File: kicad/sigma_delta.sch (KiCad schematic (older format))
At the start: 26 parts, among them U1801 SI8661BD, U1802 SI8661BD

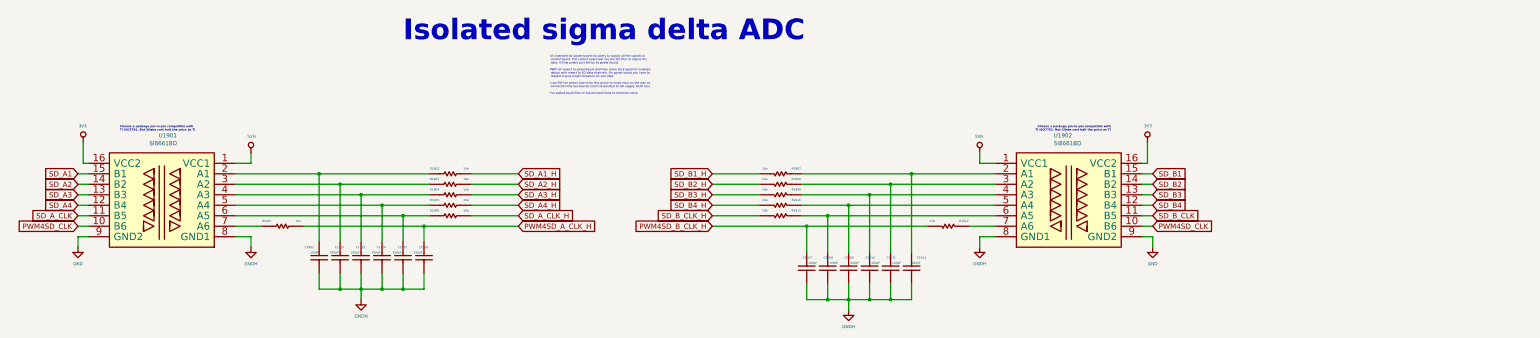
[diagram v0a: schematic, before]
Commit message: changing single row terminal block to double row
I've changed to double row all the connectors, RJ45 and terminal blocks,
I saves spaces and also make it more intuitive related to user
interface..lets go
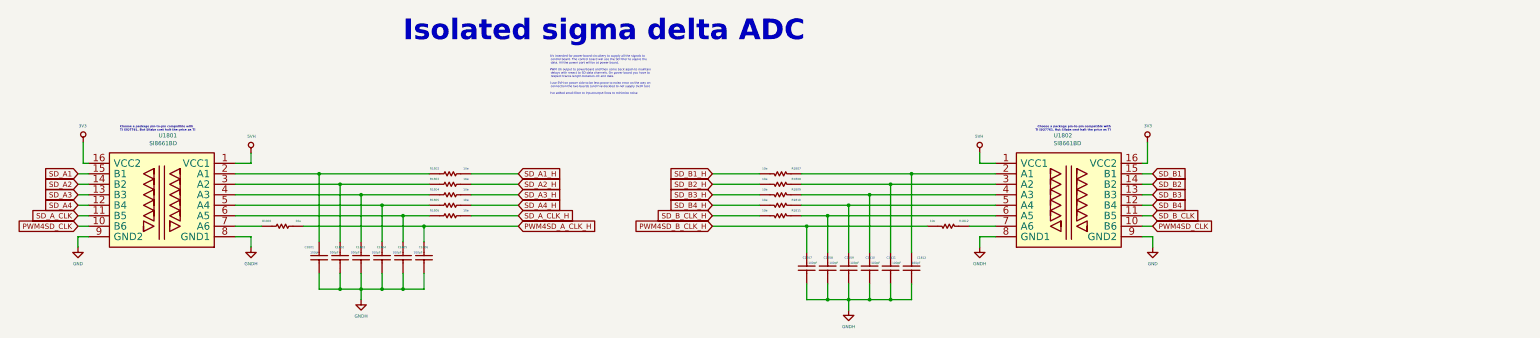
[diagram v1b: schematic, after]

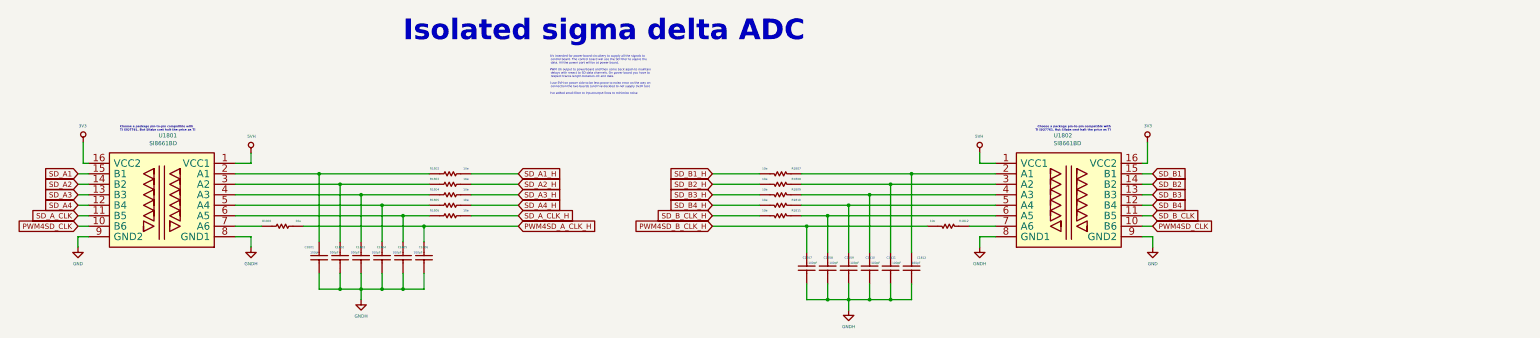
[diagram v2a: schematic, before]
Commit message: I forgot that QUEP was diferential!! all to back....
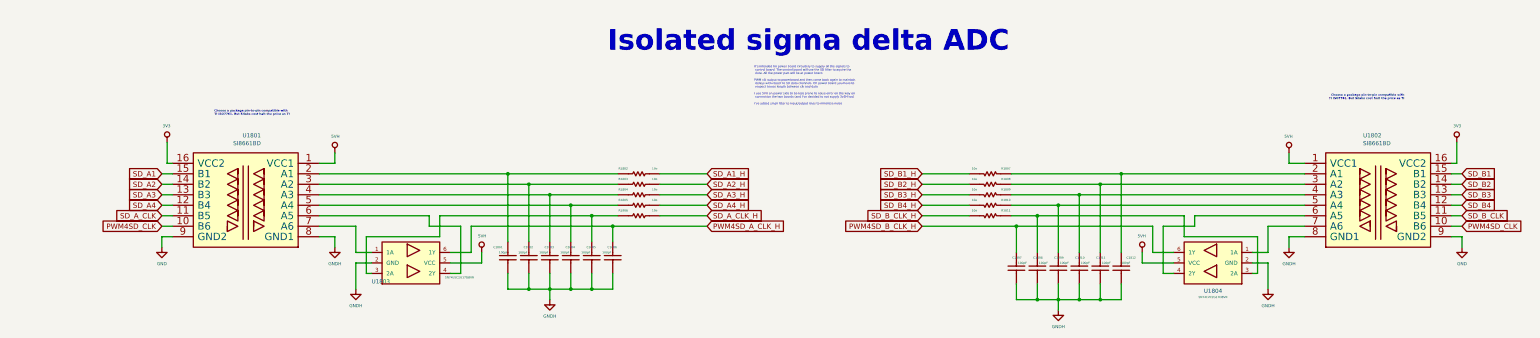
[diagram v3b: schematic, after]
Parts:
- removed R1801, R1812: 10e, Resistor_SMD:R_0603_1608Metric, symbol servo:Resistor
- added U1803, U1804: SN74LVC2G17DBVR, servo:SOT-23-6, symbol servo:SN74LVC2G17DBVR
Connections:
- net 5VH: now also U1803.5 (VCC), U1804.5 (VCC)
- net GNDH: now also U1803.2 (GND), U1804.2 (GND)
- net PWM4SD_A_CLK_H: now also U1803.6 (1Y)
- net PWM4SD_B_CLK_H: now also U1804.6 (1Y)
- net at C1805.1, R1806.1: now also U1803.3 (2A); no longer U1801.6 (A5)
- net at U1801.7 (A6): now also U1803.1 (1A)
- net at C1808.1, R1811.1: now also U1804.3 (2A); no longer U1802.6 (A5)
- net at U1802.7 (A6): now also U1804.1 (1A)
- new net: U1801.6 (A5), U1803.4 (2Y)
- new net: U1802.6 (A5), U1804.4 (2Y)
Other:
- moved on the sheet: C1801, C1802, C1803, C1804, C1805, C1806, C1807, C1808, C1809, C1810, C1811, C1812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

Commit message: placing smmall capacitors and resistors nerar his group
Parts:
- added C1813, C1814, C1815, C1816, C1817, C1818: 100pF, servo:C_0603_1608Metric, symbol servo:Capacitor
- added R1801, R1812: 10e, Resistor_SMD:R_0603_1608Metric, symbol servo:Resistor
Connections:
- net 3V3: now also C1813.1, C1818.1
- net 5VH: now also C1814.1, C1815.1, C1816.1, C1817.1
- net GND: now also C1813.2 (Capacitor), C1818.2 (Capacitor)
- net GNDH: now also C1814.2 (Capacitor), C1815.2 (Capacitor), C1816.2 (Capacitor), C1817.2 (Capacitor)
- net PWM4SD_A_CLK_H: now also R1801.2; no longer U1803.6 (1Y)
- net PWM4SD_B_CLK_H: now also R1812.2; no longer U1804.6 (1Y)
- new net: R1812.1, U1804.6 (1Y)
- new net: R1801.1, U1803.6 (1Y)
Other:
- moved on the sheet: C1806, C1807

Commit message: beginine routing... far far away
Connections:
- net PWM4SD_A_CLK_H renamed SD_CLK_OUT1_H
- net PWM4SD_B_CLK_H renamed SD_CLK_OUT2_H
- net PWM4SD_CLK renamed SD_CLK_OUT
- net SD_A1 renamed SD1_U
- net SD_A1_H renamed SD1_U_H
- net SD_A2 renamed SD1_V
- net SD_A2_H renamed SD1_V_H
- net SD_A3 renamed SD1_W
- net SD_A3_H renamed SD1_W_H
- net SD_A4 renamed SD1_A
- net SD_A4_H renamed SD1_A_H
- net SD_A_CLK renamed SD_CLK_IN1
- net SD_A_CLK_H renamed SD_CLK_IN1_H
- net SD_B1 renamed SD2_U
- net SD_B1_H renamed SD2_U_H
- net SD_B2 renamed SD2_V
- net SD_B2_H renamed SD2_V_H
- net SD_B3 renamed SD2_W
- net SD_B3_H renamed SD2_W_H
- net SD_B4 renamed SD2_A
- net SD_B4_H renamed SD2_A_H
- net SD_B_CLK renamed SD_CLK_IN2
- net SD_B_CLK_H renamed SD_CLK_IN2_H
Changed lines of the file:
@@
 Isolated sigma delta ADC
 Text GLabel 2700 3350 0    50   Input ~ 0
-SD_A_CLK
+SD_CLK_IN1
 $Comp
 L servo:GND #PWR?
@@
 	-1   0    0    -1
 $EndComp
-Text GLabel 2700 3450 0    50   Input ~ 0
-PWM4SD_CLK
 $Comp
 L servo:3V3 #PWR?
@@
 	2750 2650 2750 2850
 Text GLabel 2700 2950 0    50   Input ~ 0
-SD_A1
+SD1_U
 Text GLabel 2700 3050 0    50   Input ~ 0
-SD_A2
+SD1_V
 Text GLabel 2700 3150 0    50   Input ~ 0
-SD_A3
+SD1_W
 Text GLabel 2700 3250 0    50   Input ~ 0
-SD_A4
+SD1_A
 $Comp
 L servo:GNDH #PWR?
@@
 Wire Wire Line
 	7450 3350 7900 3350
-Text GLabel 15100 3350 2    50   Input ~ 0
-SD_B_CLK
 $Comp
 L servo:GND #PWR?
@@
 	1    0    0    -1
 $EndComp
-Text GLabel 15100 3450 2    50   Input ~ 0
-PWM4SD_CLK
 $Comp
 L servo:3V3 #PWR?
@@
 Wire Wire Line
 	15050 2650 15050 2850
-Text GLabel 15100 2950 2    50   Input ~ 0
-SD_B1
-Text GLabel 15100 3050 2    50   Input ~ 0
-SD_B2
-Text GLabel 15100 3150 2    50   Input ~ 0
-SD_B3
-Text GLabel 15100 3250 2    50   Input ~ 0
-SD_B4
 $Comp
 L servo:GNDH #PWR?
@@
 Wire Wire Line
 	11250 4250 11250 4150
-Text GLabel 7900 2950 2    50   Input ~ 0
-SD_A1_H
-Text GLabel 7900 3050 2    50   Input ~ 0
-SD_A2_H
-Text GLabel 7900 3150 2    50   Input ~ 0
-SD_A3_H
-Text GLabel 7900 3250 2    50   Input ~ 0
-SD_A4_H
-Text GLabel 7900 3350 2    50   Input ~ 0
-SD_A_CLK_H
-Text GLabel 7900 3450 2    50   Input ~ 0
-PWM4SD_A_CLK_H
-Text GLabel 9950 2950 0    50   Input ~ 0
-SD_B1_H
-Text GLabel 9950 3050 0    50   Input ~ 0
-SD_B2_H
-Text GLabel 9950 3150 0    50   Input ~ 0
-SD_B3_H
-Text GLabel 9950 3250 0    50   Input ~ 0
-SD_B4_H
-Text GLabel 9950 3350 0    50   Input ~ 0
-SD_B_CLK_H
-Text GLabel 9950 3450 0    50   Input ~ 0
-PWM4SD_B_CLK_H
 $Comp
 L servo:SN74LVC2G17DBVR U?
@@
 AR Path="/5EC40F3C/5E3CAD23" Ref="C?"  Part="1"
 AR Path="/6056AA11/5E3CAD23" Ref="C1818"  Part="1"
-F 0 "C1818" V 15400 2700 20  0000 R CNN
-F 1 "100pF" V 15350 2750 20  0000 R CNN
+F 0 "C1818" V 15322 2540 20  0000 R CNN
+F 1 "100pF" V 15279 2540 20  0000 R CNN
 F 2 "servo:C_0603_1608Metric" H 15250 2550 60  0001 C CNN
 F 3 "" H 15250 2650 60  0000 C CNN
@@
 AR Path="/6056AA11/5E3CAD30" Ref="#PWR0245"  Part="1"
 F 0 "#PWR0245" H 15250 2500 30  0001 C CNN
-F 1 "GND" H 15250 2592 30  0000 C CNN
+F 1 "GND" H 15150 2700 30  0000 C CNN
 F 2 "" H 15250 2750 50  0001 C CNN
 F 3 "" H 15250 2750 50  0001 C CNN
@@
 	1    0    0    -1
 $EndComp
+Text GLabel 2700 3450 0    50   Input ~ 0
+SD_CLK_OUT
+Text GLabel 15100 3350 2    50   Input ~ 0
+SD_CLK_IN2
+Text GLabel 15100 2950 2    50   Input ~ 0
+SD2_U
+Text GLabel 15100 3050 2    50   Input ~ 0
+SD2_V
+Text GLabel 15100 3150 2    50   Input ~ 0
+SD2_W
+Text GLabel 15100 3250 2    50   Input ~ 0
+SD2_A
+Text GLabel 15100 3450 2    50   Input ~ 0
+SD_CLK_OUT
+Text GLabel 9950 3350 0    50   Input ~ 0
+SD_CLK_IN2_H
+Text GLabel 9950 2950 0    50   Input ~ 0
+SD2_U_H
+Text GLabel 9950 3050 0    50   Input ~ 0
+SD2_V_H
+Text GLabel 9950 3150 0    50   Input ~ 0
+SD2_W_H
+Text GLabel 9950 3250 0    50   Input ~ 0
+SD2_A_H
+Text GLabel 9950 3450 0    50   Input ~ 0
+SD_CLK_OUT2_H
+Text GLabel 7900 3350 2    50   Input ~ 0
+SD_CLK_IN1_H
+Text GLabel 7900 2950 2    50   Input ~ 0
+SD1_U_H
+Text GLabel 7900 3050 2    50   Input ~ 0
+SD1_V_H
+Text GLabel 7900 3150 2    50   Input ~ 0
+SD1_W_H
+Text GLabel 7900 3250 2    50   Input ~ 0
+SD1_A_H
+Text GLabel 7900 3450 2    50   Input ~ 0
+SD_CLK_OUT1_H
 $EndSCHEMATC

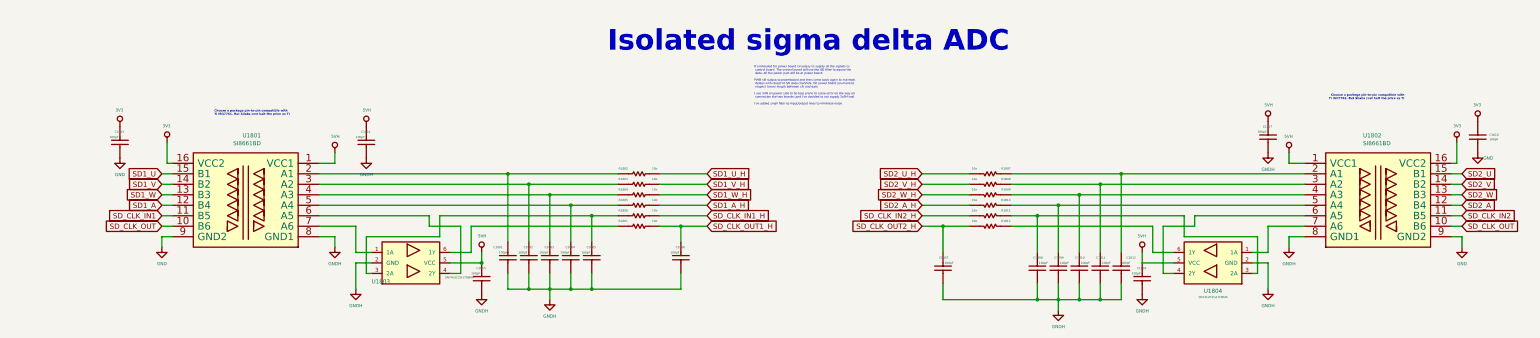
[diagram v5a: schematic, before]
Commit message: change in 5v interface scenario.. remove bridges
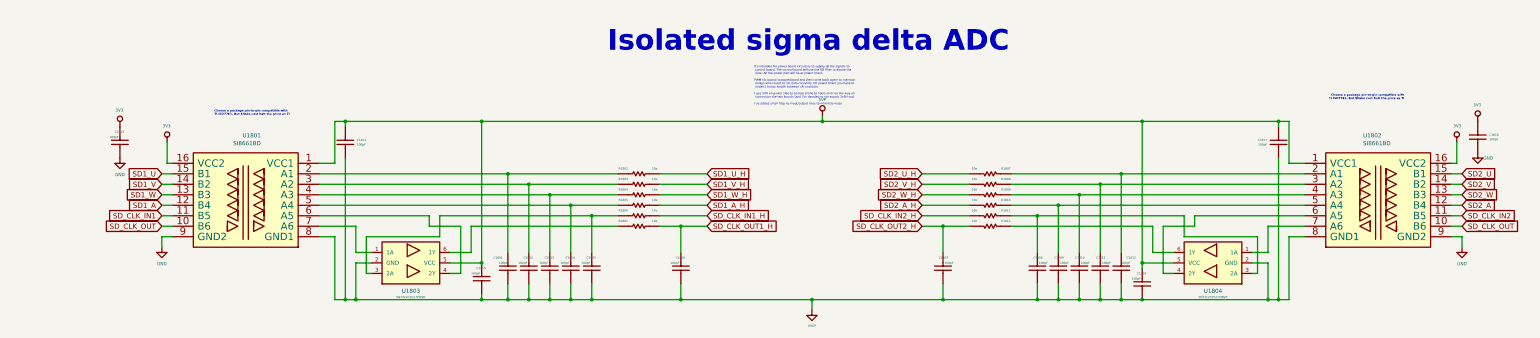
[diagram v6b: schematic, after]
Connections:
- net 5VH renamed 5VP
- net GNDH renamed GNDP
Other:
- moved on the sheet: C1801, C1802, C1803, C1804, C1805, C1806, C1814, C1816, C1817

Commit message: serigrafia...
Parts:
- R1801, R1802, R1803, R1804, R1805, R1806, R1807, R1808, R1809, R1810, R1811, R1812: footprint Resistor_SMD:R_0603_1608Metric -> servo:R_0603_1608Metric
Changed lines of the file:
@@
 F 0 "R1802" H 7100 3000 20  0000 C CNN
 F 1 "10e" H 7400 3000 20  0000 C CNN
-F 2 "Resistor_SMD:R_0603_1608Metric" H 6750 2850 60  0001 C CNN
+F 2 "servo:R_0603_1608Metric" H 6750 2850 60  0001 C CNN
 F 3 "" H 6850 2950 60  0001 C CNN
 	1    7250 2950
@@
 F 0 "R1803" H 7100 3100 20  0000 C CNN
 F 1 "10e" H 7400 3100 20  0000 C CNN
-F 2 "Resistor_SMD:R_0603_1608Metric" H 6750 2950 60  0001 C CNN
+F 2 "servo:R_0603_1608Metric" H 6750 2950 60  0001 C CNN
 F 3 "" H 6850 3050 60  0001 C CNN
 	1    7250 3050
@@
 F 0 "R1804" H 7100 3200 20  0000 C CNN
 F 1 "10e" H 7400 3200 20  0000 C CNN
-F 2 "Resistor_SMD:R_0603_1608Metric" H 6750 3050 60  0001 C CNN
+F 2 "servo:R_0603_1608Metric" H 6750 3050 60  0001 C CNN
 F 3 "" H 6850 3150 60  0001 C CNN
 	1    7250 3150
@@
 F 0 "R1805" H 7100 3300 20  0000 C CNN
 F 1 "10e" H 7400 3300 20  0000 C CNN
-F 2 "Resistor_SMD:R_0603_1608Metric" H 6750 3150 60  0001 C CNN
+F 2 "servo:R_0603_1608Metric" H 6750 3150 60  0001 C CNN
 F 3 "" H 6850 3250 60  0001 C CNN
 	1    7250 3250
@@
 F 0 "R1806" H 7100 3400 20  0000 C CNN
 F 1 "10e" H 7400 3400 20  0000 C CNN
-F 2 "Resistor_SMD:R_0603_1608Metric" H 6750 3250 60  0001 C CNN
+F 2 "servo:R_0603_1608Metric" H 6750 3250 60  0001 C CNN
 F 3 "" H 6850 3350 60  0001 C CNN
 	1    7250 3350
@@
 F 0 "R1807" H 10450 3000 20  0000 C CNN
 F 1 "10e" H 10750 3000 20  0000 C CNN
-F 2 "Resistor_SMD:R_0603_1608Metric" H 10100 2850 60  0001 C CNN
+F 2 "servo:R_0603_1608Metric" H 10100 2850 60  0001 C CNN
 F 3 "" H 10200 2950 60  0001 C CNN
 	1    10600 2950
@@
 F 0 "R1808" H 10450 3100 20  0000 C CNN
 F 1 "10e" H 10750 3100 20  0000 C CNN
-F 2 "Resistor_SMD:R_0603_1608Metric" H 10100 2950 60  0001 C CNN
+F 2 "servo:R_0603_1608Metric" H 10100 2950 60  0001 C CNN
 F 3 "" H 10200 3050 60  0001 C CNN
 	1    10600 3050
@@
 F 0 "R1809" H 10450 3200 20  0000 C CNN
 F 1 "10e" H 10750 3200 20  0000 C CNN
-F 2 "Resistor_SMD:R_0603_1608Metric" H 10100 3050 60  0001 C CNN
+F 2 "servo:R_0603_1608Metric" H 10100 3050 60  0001 C CNN
 F 3 "" H 10200 3150 60  0001 C CNN
 	1    10600 3150
@@
 F 0 "R1810" H 10450 3300 20  0000 C CNN
 F 1 "10e" H 10750 3300 20  0000 C CNN
-F 2 "Resistor_SMD:R_0603_1608Metric" H 10100 3150 60  0001 C CNN
+F 2 "servo:R_0603_1608Metric" H 10100 3150 60  0001 C CNN
 F 3 "" H 10200 3250 60  0001 C CNN
 	1    10600 3250
@@
 F 0 "R1811" H 10450 3400 20  0000 C CNN
 F 1 "10e" H 10750 3400 20  0000 C CNN
-F 2 "Resistor_SMD:R_0603_1608Metric" H 10100 3250 60  0001 C CNN
+F 2 "servo:R_0603_1608Metric" H 10100 3250 60  0001 C CNN
 F 3 "" H 10200 3350 60  0001 C CNN
 	1    10600 3350
@@
 F 0 "R1812" H 10450 3500 20  0000 C CNN
 F 1 "10e" H 10750 3500 20  0000 C CNN
-F 2 "Resistor_SMD:R_0603_1608Metric" H 10100 3350 60  0001 C CNN
+F 2 "servo:R_0603_1608Metric" H 10100 3350 60  0001 C CNN
 F 3 "" H 10200 3450 60  0001 C CNN
 	1    10600 3450
@@
 F 0 "R1801" H 7100 3500 20  0000 C CNN
 F 1 "10e" H 7400 3500 20  0000 C CNN
-F 2 "Resistor_SMD:R_0603_1608Metric" H 6750 3350 60  0001 C CNN
+F 2 "servo:R_0603_1608Metric" H 6750 3350 60  0001 C CNN
 F 3 "" H 6850 3450 60  0001 C CNN
 	1    7250 3450

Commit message: serigraphi, improve of nets. change of soic 8 footprint
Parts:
- U1801, U1802: footprint Package_SO:SOIC-16W_7.5x10.3mm_P1.27mm -> servo:SOIC-16W_7.5x10.3mm_P1.27mm
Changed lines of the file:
@@
 F 0 "U1801" H 3356 3693 39  0000 L BNN
 F 1 "SI8661BD" H 3356 3618 39  0000 L BNN
-F 2 "Package_SO:SOIC-16W_7.5x10.3mm_P1.27mm" H 2900 3450 60  0001 C CNN
+F 2 "servo:SOIC-16W_7.5x10.3mm_P1.27mm" H 2900 3450 60  0001 C CNN
 F 3 "../doc/datasheets/Si8660.pdf" H 3400 3750 60  0001 C CNN
 	1    3500 3150
@@
 F 0 "U1802" H 14156 3693 39  0000 L BNN
 F 1 "SI8661BD" H 14156 3618 39  0000 L BNN
-F 2 "Package_SO:SOIC-16W_7.5x10.3mm_P1.27mm" H 13700 3450 60  0001 C CNN
+F 2 "servo:SOIC-16W_7.5x10.3mm_P1.27mm" H 13700 3450 60  0001 C CNN
 F 3 "../doc/datasheets/Si8660.pdf" H 14200 3750 60  0001 C CNN
 	1    14300 3150
